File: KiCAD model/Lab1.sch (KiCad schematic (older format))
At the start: 98 parts, among them J1 USB_OTG, J2 SWD, SW1 1825910-6, SW10 Rotary_Encoder, U1 PMW3389, U2 AP2125N-3.3TRG, U3 MIC5235YM5-TR, U4 STM32F411RETx, U5 USBLC6-2SC6, Y1 16Mhz

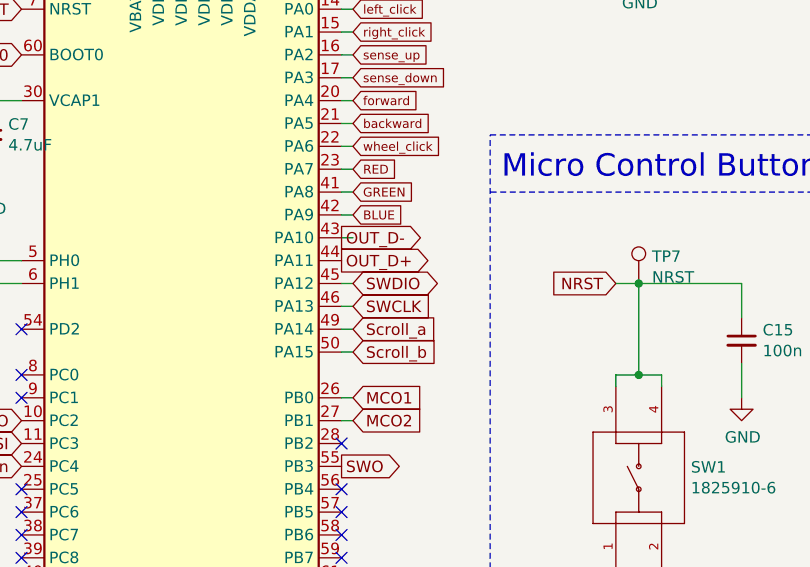
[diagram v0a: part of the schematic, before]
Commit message: fix swdio/swclk + usb issue
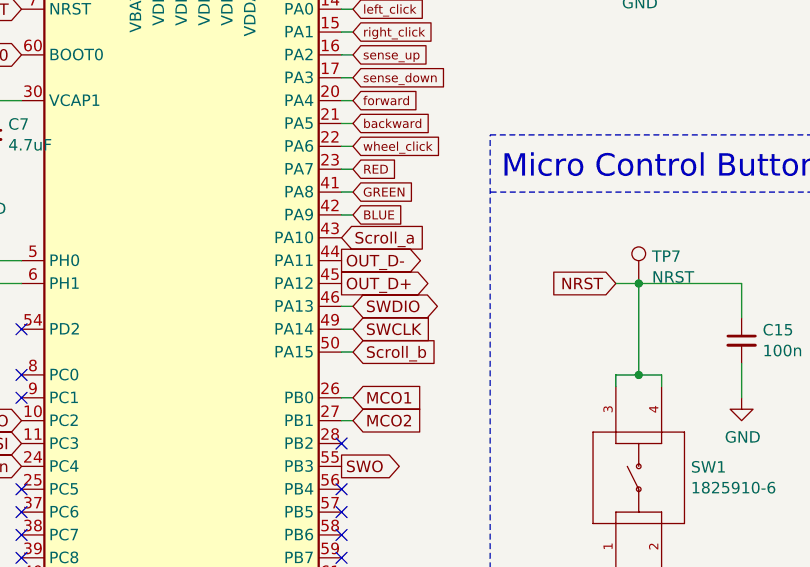
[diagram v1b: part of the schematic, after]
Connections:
- net OUT_D+: now also U4.45 (PA12); no longer U4.44 (PA11)
- net OUT_D-: now also U4.44 (PA11); no longer U4.43 (PA10)
- net SWCLK: now also U4.49 (PA14); no longer U4.46 (PA13)
- net SWDIO: now also U4.46 (PA13); no longer U4.45 (PA12)
- net Scroll_a: now also U4.43 (PA10); no longer U4.49 (PA14)
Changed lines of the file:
@@
 Wire Wire Line
 	6800 2400 6800 2600
-Text GLabel 8900 2700 2    50   BiDi ~ 0
+Text GLabel 8900 2800 2    50   BiDi ~ 0
 SWDIO
-Text GLabel 8900 2800 2    50   Input ~ 0
+Text GLabel 8900 2900 2    50   Input ~ 0
 SWCLK
 Wire Wire Line
@@
 Text GLabel 7450 3400 0    50   Input ~ 0
 MOSI
+Text GLabel 8850 2700 2    50   Output ~ 0
+OUT_D+
 Text GLabel 8850 2600 2    50   Output ~ 0
-OUT_D+
-Text GLabel 8850 2500 2    50   Output ~ 0
 OUT_D-
 Text GLabel 8850 3500 2    50   Output ~ 0
@@
 Wire Wire Line
 	8850 2400 8900 2400
-Wire Wire Line
-	8900 2500 8850 2500
 $Comp
 L Connector:Conn_01x06_Male J2
@@
 Wire Wire Line
 	4650 2500 4650 2450
-Wire Wire Line
-	8900 2700 8850 2700
-Text GLabel 8900 2900 2    50   Input ~ 0
+Text GLabel 8850 2500 2    50   Input ~ 0
 Scroll_a
 Text GLabel 8900 3000 2    50   Input ~ 0
